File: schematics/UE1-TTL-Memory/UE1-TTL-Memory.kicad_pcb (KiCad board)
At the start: 2 copper layers, 76.8 x 99.1 mm, 53 parts, among them J1 Edge 1, J2 Edge 2, SW1 Inputs, SW2 Select Program, U1 74LS139, U2 74LS259, U3 74LS151, U4 74LS125, U5 74LS151, U6 74LS259, U7 74LS393, U8 74LS393, U9 28C256

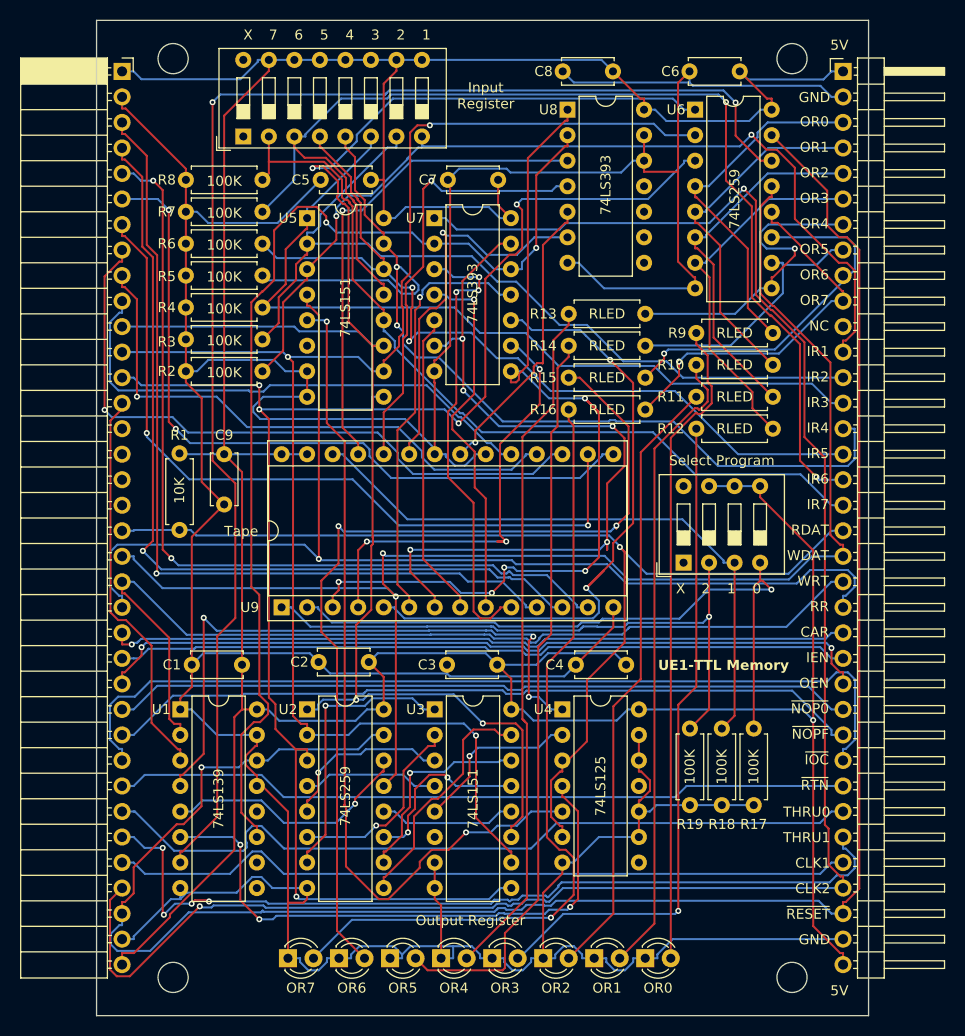
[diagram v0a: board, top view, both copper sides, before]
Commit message: Add a tape "REWIND" opcode to reset the PC early
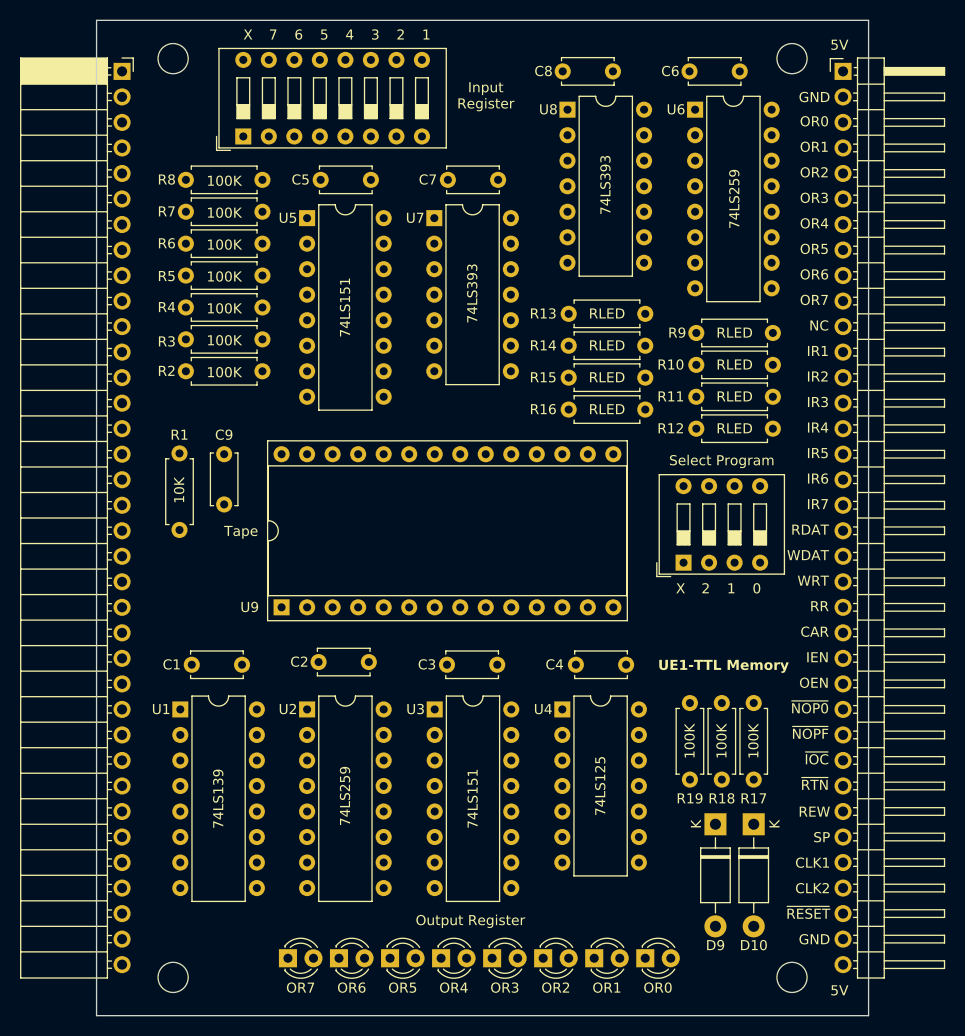
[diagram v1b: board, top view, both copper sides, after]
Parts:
- added D10: 1N5819, Diode_THT:D_DO-41_SOD81_P10.16mm_Horizontal, F.Cu at (153.0, 128.3)
- added D9: 1N5819, Diode_THT:D_DO-41_SOD81_P10.16mm_Horizontal, F.Cu at (149.2, 128.3)
- moved R17 2.54 mm to (153.0, 116.2)
- moved R18 2.54 mm to (149.9, 116.2)
- moved R19 2.54 mm to (146.7, 116.2)
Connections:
- net THRU0 renamed REWIND
- net THRU1 renamed SPARE
- U7 pad 12: RESET -> REWIND_TAPE
- U7 pad 2: RESET -> REWIND_TAPE
- U8 pad 2: RESET -> REWIND_TAPE
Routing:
- net GND: track 482.1 -> 0.00 mm
- net +5V: track 372.8 -> 0.00 mm, vias 1 -> 0
- net ~{RESET}: track 200.5 -> 0.00 mm, vias 1 -> 0
- net CLK2: track 193.0 -> 0.00 mm, vias 2 -> 0
- net MEM0: track 161.9 -> 0.00 mm, vias 3 -> 0
- net MEM2: track 158.0 -> 0.00 mm, vias 5 -> 0
- net MEM1: track 152.0 -> 0.00 mm, vias 3 -> 0
- net WR_DATA: track 142.2 -> 0.00 mm, vias 2 -> 0
- net ~{WR_OR}: track 140.2 -> 0.00 mm, vias 2 -> 0
- net IR6: track 118.6 -> 0.00 mm, vias 2 -> 0
- net RR: track 113.6 -> 0.00 mm, vias 1 -> 0
- net RD_DATA: track 108.8 -> 0.00 mm, vias 1 -> 0
- net RESET: track 108.2 -> 0.00 mm, vias 2 -> 0
- net IR4: track 97.5 -> 0.00 mm, vias 2 -> 0
- net Net-(U7B-Q3): track 95.7 -> 0.00 mm, vias 5 -> 0
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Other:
- board text added: "REW"
- board text added: "SP"
- board text removed: "THRU0"
- board text removed: "THRU1"

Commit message: Lay out memory board
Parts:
- removed the C2 at (114.7, 112.1)
- removed D10, D9: 1N5819, Diode_THT:D_DO-41_SOD81_P10.16mm_Horizontal
- removed the U5 at (108.6, 67.9)
- added C8: 100nF, Capacitor_THT:C_Disc_D5.0mm_W2.5mm_P5.00mm, F.Cu at (140.3, 112.4)
- added U8: 74LS32, Package_DIP:DIP-14_W7.62mm, F.Cu at (134.0, 116.8)
- SW1: footprint Button_Switch_THT:SW_DIP_SPSTx08_Slide_9.78x22.5mm_W7.62mm_P2.54mm -> Button_Switch_THT:SW_DIP_SPSTx08_Slide_6.7x21.88mm_W7.62mm_P2.54mm_LowProfile
- SW2: footprint Button_Switch_THT:SW_DIP_SPSTx04_Slide_9.78x12.34mm_W7.62mm_P2.54mm -> Button_Switch_THT:SW_DIP_SPSTx03_Slide_6.7x9.18mm_W7.62mm_P2.54mm_LowProfile
- U3: value 74LS151 -> 74LS251
- U4: value 74LS125 -> 74LS251; footprint Package_DIP:DIP-14_W7.62mm -> Package_DIP:DIP-16_W7.62mm
- moved R9 57.2 mm to (154.9, 136.5)
- moved U4 55.1 mm to (108.6, 67.9)
- moved R10 50.8 mm to (154.9, 133.3)
- moved R13 48.1 mm to (154.9, 123.8)
- moved R11 44.5 mm to (154.9, 130.2)
- moved R14 42.0 mm to (154.9, 120.7)
- moved R12 38.1 mm to (154.9, 127.0)
- moved R15 36.0 mm to (154.9, 117.5)
- moved R16 30.1 mm to (154.9, 114.3)
- moved R8 19.1 mm to (103.5, 83.2)
- moved C7 17.7 mm to (153.0, 64.1)
- moved U5 17.1 mm to (133.9, 67.9)
- moved U7 16.2 mm to (146.5, 67.9)
- moved C5 15.6 mm to (140.3, 64.1)
- moved SW1 14.6 mm to (116.8, 59.8)
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- renumbered C4 to C2, C5 to C4, C6 to C5, C7 to C6, C8 to C7, U6 to U5, U7 to U6, U8 to U7
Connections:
- J1 pad 15: INST0 -> unconnected-(J1-Pin_15-Pad15)
- J1 pad 16: INST1 -> unconnected-(J1-Pin_16-Pad16)
- J1 pad 17: INST2 -> unconnected-(J1-Pin_17-Pad17)
- J1 pad 18: INST3 -> unconnected-(J1-Pin_18-Pad18)
- SW1 pad 1: unconnected-(SW1-Pad1) -> IR7
- SW1 pad 16: unconnected-(SW1-Pad16) -> +5V
- SW1 pad 2: IR7 -> IR6
- SW1 pad 3: IR6 -> IR5
- SW1 pad 4: IR5 -> IR4
- SW1 pad 5: IR4 -> IR3
- SW1 pad 6: IR3 -> IR2
- SW1 pad 7: IR2 -> IR1
- SW1 pad 8: IR1 -> unconnected-(SW1-Pad8)
- SW1 pad 9: +5V -> unconnected-(SW1-Pad9)
- SW2 pad 1: unconnected-(SW2-Pad1) -> PGM2
- SW2 pad 2: PGM2 -> PGM1
- SW2 pad 3: PGM1 -> PGM0
- SW2 pad 4: PGM0 -> +5V
- U3 pad 5: Net-(U3-Z) -> RD_DATA
- U3 pad 7: GND -> ~{RD_SR}
- U4 pad 1: ~{RD_SR} -> IR3
- U4 pad 10: GND -> MEM1
- U4 pad 11: unconnected-(U4-Pad11) -> MEM0
- U4 pad 12: GND -> IR7
- U4 pad 13: GND -> IR6
- U4 pad 14: +5V -> IR5
- U4 pad 2: Net-(U3-Z) -> IR2
- U4 pad 3: RD_DATA -> IR1
- U4 pad 4: ~{RD_IR} -> RR
- U4 pad 5: Net-(U5-Z) -> RD_DATA
- U4 pad 6: RD_DATA -> unconnected-(U4-~{Y}-Pad6)
- U4 pad 7: GND -> ~{RD_IR}
- U4 pad 8: unconnected-(U4-Pad8) -> GND
- U4 pad 9: GND -> MEM2
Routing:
- net GND: track 0.00 -> 500.1 mm, vias 0 -> 1
- net +5V: track 0.00 -> 372.5 mm, vias 0 -> 1
- net ~{RESET}: track 0.00 -> 173.6 mm, vias 0 -> 2
- net CLK2: track 0.00 -> 169.2 mm, vias 0 -> 2
- net MEM0: track 0.00 -> 147.9 mm, vias 0 -> 3
- net MEM1: track 0.00 -> 135.0 mm, vias 0 -> 2
- net MEM2: track 0.00 -> 135.0 mm, vias 0 -> 3
- net RD_DATA: track 0.00 -> 130.4 mm, vias 0 -> 1
- net WR_DATA: track 0.00 -> 129.6 mm, vias 0 -> 3
- net OR0: track 0.00 -> 125.2 mm, vias 0 -> 1
- net OR1: track 0.00 -> 120.9 mm, vias 0 -> 2
- net RR: track 0.00 -> 108.1 mm, vias 0 -> 1
- net IR6: track 0.00 -> 105.0 mm, vias 0 -> 1
- net OR2: track 0.00 -> 102.3 mm, vias 0 -> 1
- net ~{OP_RTN}: track 0.00 -> 100.2 mm, vias 0 -> 2
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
